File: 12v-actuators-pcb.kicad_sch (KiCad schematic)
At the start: 10 parts, among them J2 3.5mm WR-TBL, J3 690367280676, J5 USB_B_Mini, J7 RGBA_LEDs, J8 CAN, U1 MCP2551-I-SN

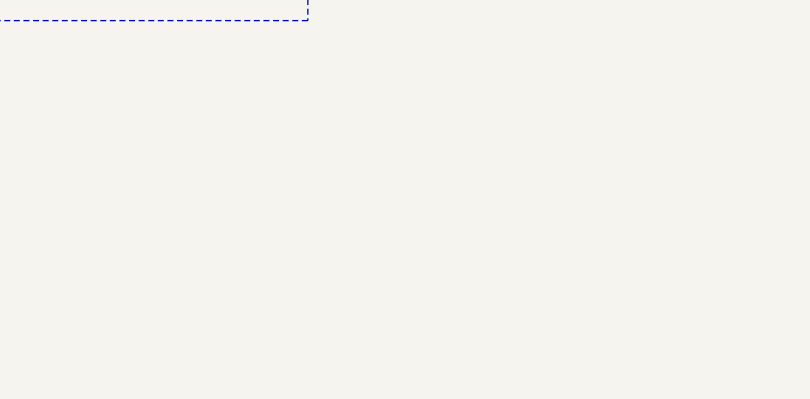
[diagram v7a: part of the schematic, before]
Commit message: placement en cours, remplacement diode schotcky, customisation empreinte capteur pression, suppression R pour les signaux figé du uC (SW, BOOT, etc). TODO avancer placement, ajouter LED
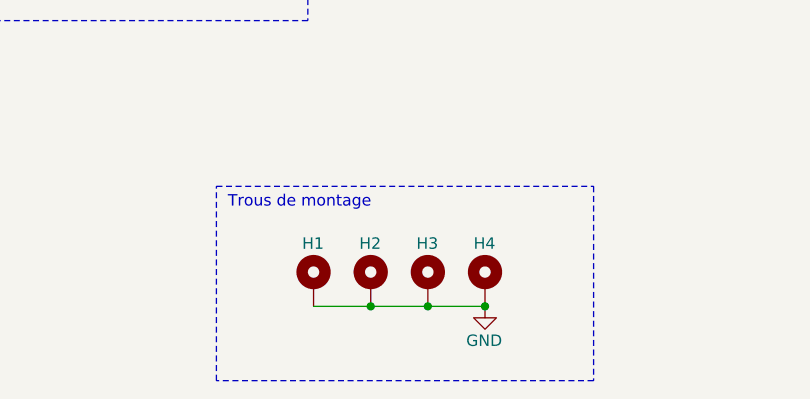
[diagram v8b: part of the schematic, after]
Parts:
- added H1, H2, H3, H4: MountingHole_Pad, MountingHole:MountingHole_3.2mm_M3_Pad, symbol Mechanical:MountingHole_Pad
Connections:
- net GND: now also H1.1, H2.1, H3.1, H4.1
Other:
- note added: "Trous de montage"
